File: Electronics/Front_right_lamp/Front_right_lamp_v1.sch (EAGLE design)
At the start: 9 parts

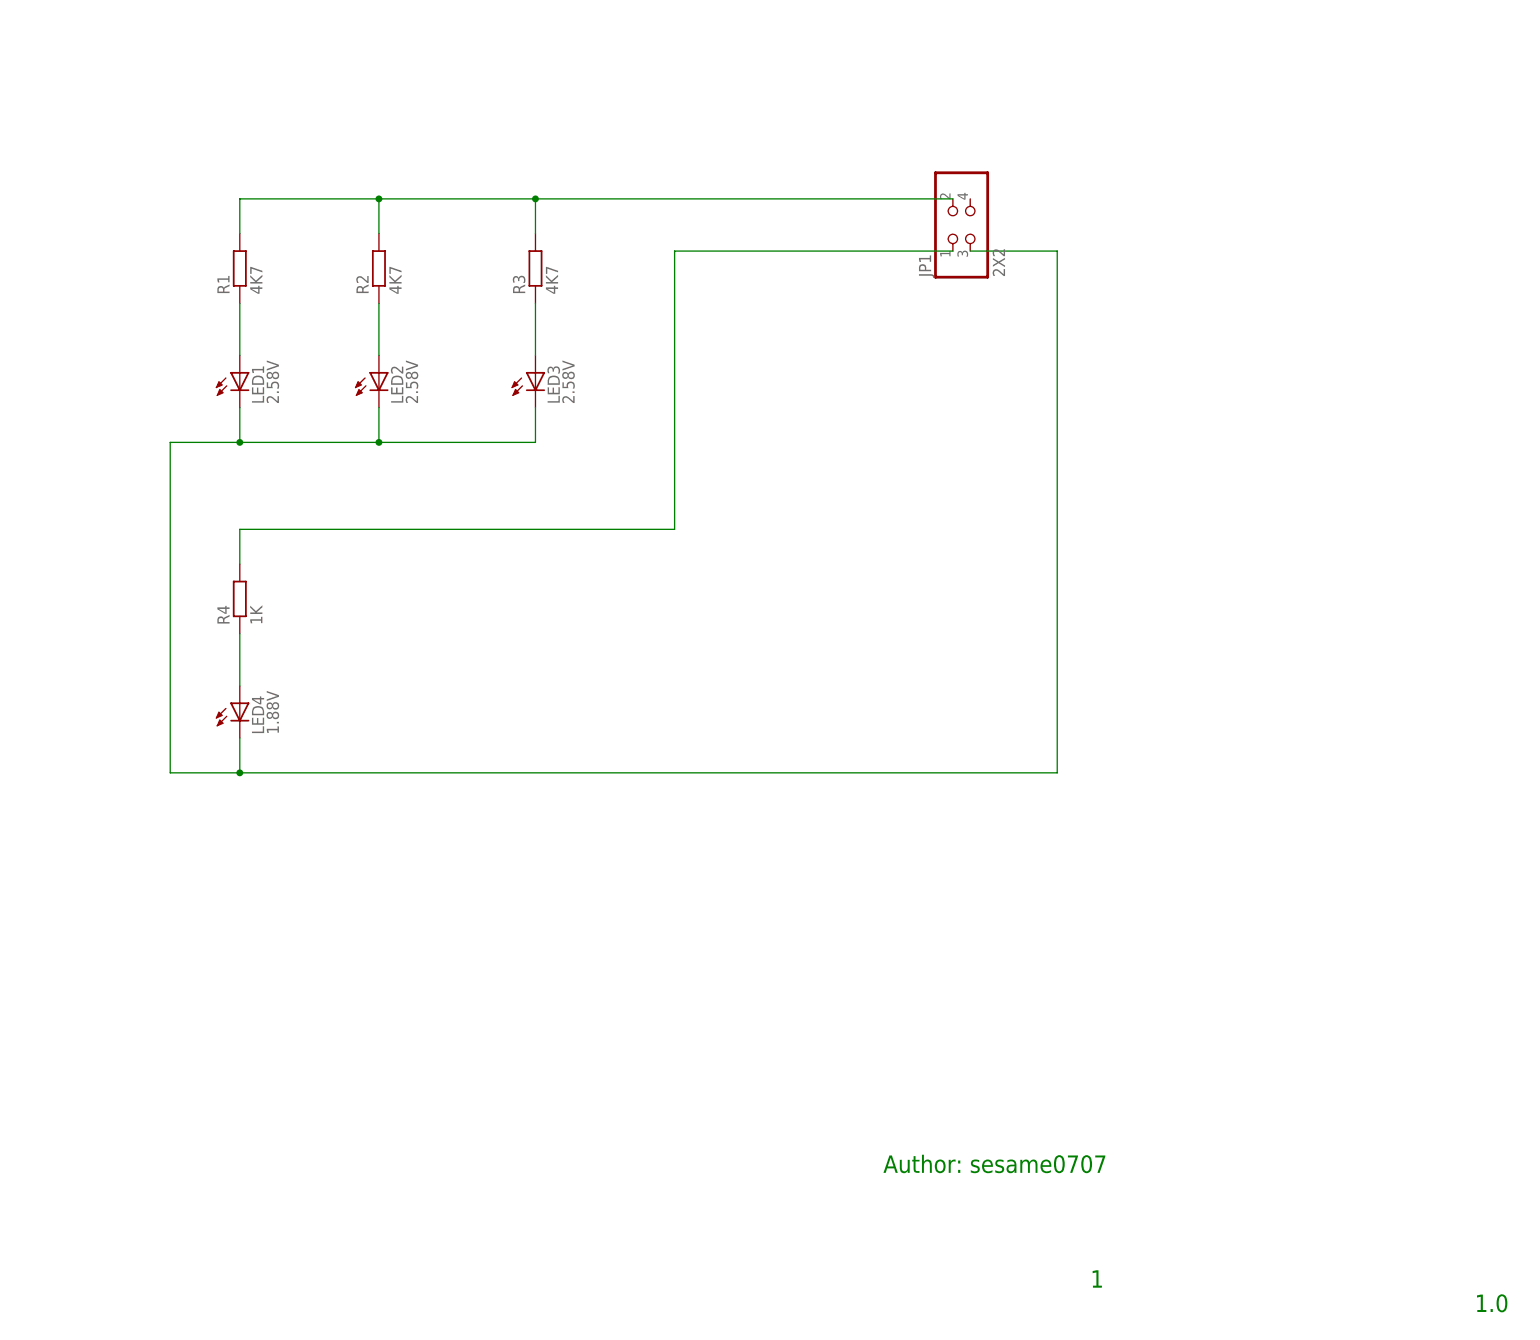
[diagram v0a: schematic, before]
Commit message: Front lamps done
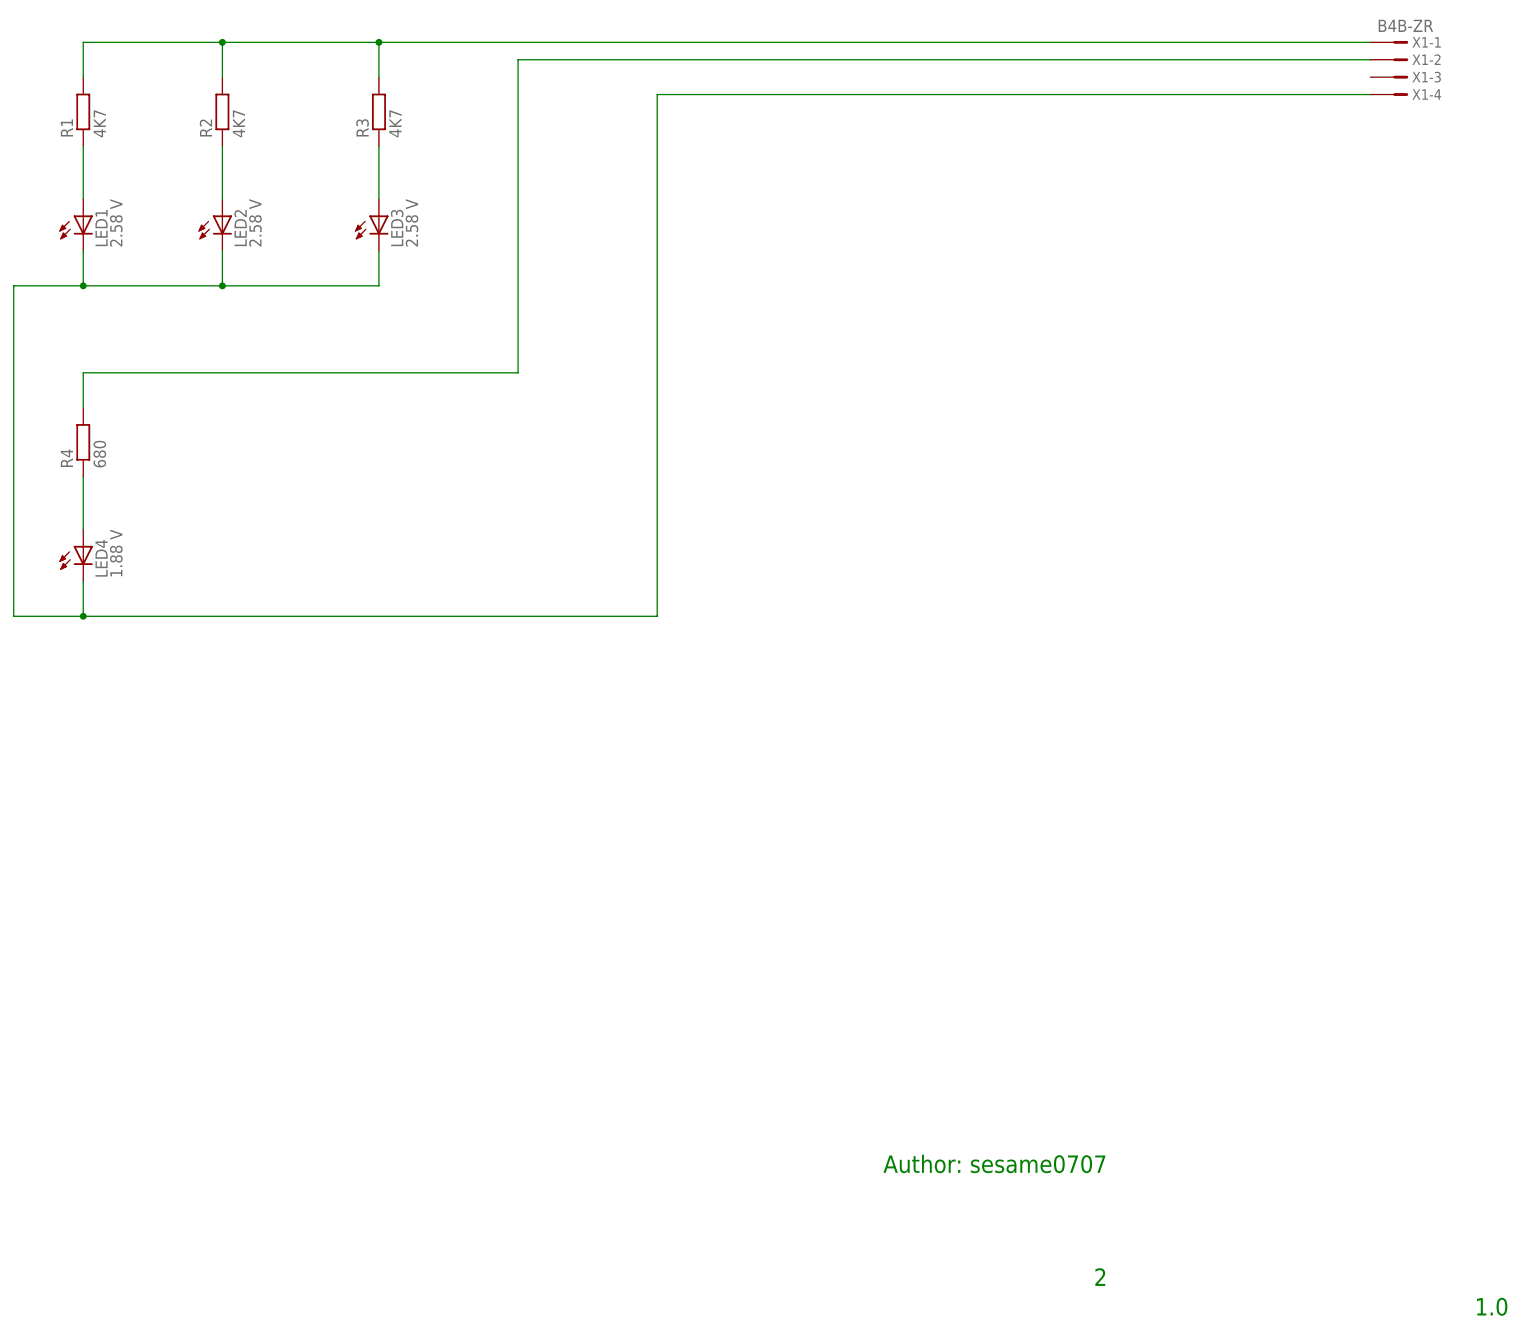
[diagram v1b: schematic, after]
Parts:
- removed JP1: 2X2, pinhead:PINHD-2X2
- added X1: B4B-ZR, con-jst:B4B-ZR
- LED1, LED2, LED3: value 2.58V -> 2.58 V; CURRENT (none) -> 0.14 mA
- LED4: value 1.88V -> 1.88 V; CURRENT (none) -> 1.42 mA
- R4: value 1K -> 680
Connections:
- net N$5: now also X1-1.1; no longer JP1.2
- net N$6: now also X1-2.1; no longer JP1.1
- net N$7: now also X1-4.1; no longer JP1.3
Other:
- note added: "2"
- note removed: "1"
- moved on the sheet: LED1, LED2, LED3, LED4, R1, R2, R3, R4
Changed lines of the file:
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@@
 <classes>
 <class number="0" name="default" width="0" drill="0">
+<clearance class="0" value="0.205"/>
 </class>
 </classes>
 <parts>
-<part name="FRAME1" library="frames" deviceset="FRAME_A_L" device="" value="Main"/>
-<part name="LED1" library="led" deviceset="LED" device="5MM" value="2.58V"/>
-<part name="LED2" library="led" deviceset="LED" device="5MM" value="2.58V"/>
-<part name="LED3" library="led" deviceset="LED" device="5MM" value="2.58V"/>
-<part name="LED4" library="led" deviceset="LED" device="5MM" value="1.88V"/>
+<part name="FRAME1" library="frames" deviceset="FRAME_A_L" device=""/>
+<part name="LED1" library="led" deviceset="LED" device="5MM" value="2.58 V">
+<attribute name="CURRENT" value="0.14 mA"/>
+</part>
+<part name="LED2" library="led" deviceset="LED" device="5MM" value="2.58 V">
+<attribute name="CURRENT" value="0.14 mA"/>
+</part>
+<part name="LED3" library="led" deviceset="LED" device="5MM" value="2.58 V">
+<attribute name="CURRENT" value="0.14 mA"/>
+</part>
+<part name="LED4" library="led" deviceset="LED" device="5MM" value="1.88 V">
+<attribute name="CURRENT" value="1.42 mA"/>
+</part>
 <part name="R1" library="resistor" deviceset="R-EU_" device="0204/2V" value="4K7"/>
 <part name="R2" library="resistor" deviceset="R-EU_" device="0204/2V" value="4K7"/>
 <part name="R3" library="resistor" deviceset="R-EU_" device="0204/2V" value="4K7"/>
-<part name="R4" library="resistor" deviceset="R-EU_" device="0204/2V" value="1K"/>
-<part name="JP1" library="pinhead" deviceset="PINHD-2X2" device="" value="2X2"/>
+<part name="R4" library="resistor" deviceset="R-EU_" device="0204/2V" value="680"/>
+<part name="X1" library="con-jst" deviceset="?4B-ZR" device="B"/>
 </parts>
 <sheets>
 <sheet>
 <plain>
-<text x="261.62" y="7.62" size="2.54" layer="91">1.0</text>
-<text x="205.486" y="11.176" size="2.54" layer="91">1</text>
 <text x="175.26" y="27.94" size="2.54" layer="91">Author: sesame0707</text>
+<text x="205.994" y="11.43" size="2.54" layer="91">2</text>
+<text x="261.62" y="7.112" size="2.54" layer="91">1.0</text>
 </plain>
 <instances>
 <instance part="FRAME1" gate="G$1" x="0" y="0"/>
 <instance part="FRAME1" gate="G$2" x="172.72" y="0"/>
-<instance part="LED1" gate="G$1" x="81.28" y="144.78"/>
-<instance part="LED2" gate="G$1" x="101.6" y="144.78"/>
-<instance part="LED3" gate="G$1" x="124.46" y="144.78"/>
-<instance part="LED4" gate="G$1" x="81.28" y="96.52"/>
-<instance part="R1" gate="G$1" x="81.28" y="160.02" rot="R90"/>
-<instance part="R2" gate="G$1" x="101.6" y="160.02" rot="R90"/>
-<instance part="R3" gate="G$1" x="124.46" y="160.02" rot="R90"/>
-<instance part="R4" gate="G$1" x="81.28" y="111.76" rot="R90"/>
-<instance part="JP1" gate="A" x="187.96" y="167.64" rot="R90"/>
+<instance part="LED1" gate="G$1" x="58.42" y="167.64">
+<attribute name="CURRENT" x="58.42" y="167.64" size="1.778" layer="96" display="off"/>
+</instance>
+<instance part="LED2" gate="G$1" x="78.74" y="167.64">
+<attribute name="CURRENT" x="78.74" y="167.64" size="1.778" layer="96" display="off"/>
+</instance>
+<instance part="LED3" gate="G$1" x="101.6" y="167.64">
+<attribute name="CURRENT" x="101.6" y="167.64" size="1.778" layer="96" display="off"/>
+</instance>
+<instance part="LED4" gate="G$1" x="58.42" y="119.38">
+<attribute name="CURRENT" x="58.42" y="119.38" size="1.778" layer="96" display="off"/>
+</instance>
+<instance part="R1" gate="G$1" x="58.42" y="182.88" rot="R90"/>
+<instance part="R2" gate="G$1" x="78.74" y="182.88" rot="R90"/>
+<instance part="R3" gate="G$1" x="101.6" y="182.88" rot="R90"/>
+<instance part="R4" gate="G$1" x="58.42" y="134.62" rot="R90"/>
+<instance part="X1" gate="-1" x="251.46" y="193.04"/>
+<instance part="X1" gate="-2" x="251.46" y="190.5"/>
+<instance part="X1" gate="-3" x="251.46" y="187.96"/>
+<instance part="X1" gate="-4" x="251.46" y="185.42"/>
 </instances>
 <busses>
@@
 <pinref part="R1" gate="G$1" pin="1"/>
 <pinref part="LED1" gate="G$1" pin="A"/>
-<wire x1="81.28" y1="154.94" x2="81.28" y2="147.32" width="0.1524" layer="91"/>
+<wire x1="58.42" y1="177.8" x2="58.42" y2="170.18" width="0.1524" layer="91"/>
 </segment>
 </net>
@@
 <pinref part="R2" gate="G$1" pin="1"/>
 <pinref part="LED2" gate="G$1" pin="A"/>
-<wire x1="101.6" y1="154.94" x2="101.6" y2="147.32" width="0.1524" layer="91"/>
+<wire x1="78.74" y1="177.8" x2="78.74" y2="170.18" width="0.1524" layer="91"/>
 </segment>
 </net>
@@
 <pinref part="R3" gate="G$1" pin="1"/>
 <pinref part="LED3" gate="G$1" pin="A"/>
-<wire x1="124.46" y1="154.94" x2="124.46" y2="147.32" width="0.1524" layer="91"/>
+<wire x1="101.6" y1="177.8" x2="101.6" y2="170.18" width="0.1524" layer="91"/>
 </segment>
 </net>
@@
 <pinref part="R4" gate="G$1" pin="1"/>
 <pinref part="LED4" gate="G$1" pin="A"/>
-<wire x1="81.28" y1="106.68" x2="81.28" y2="99.06" width="0.1524" layer="91"/>
+<wire x1="58.42" y1="129.54" x2="58.42" y2="121.92" width="0.1524" layer="91"/>
 </segment>
 </net>
@@
 <segment>
 <pinref part="R1" gate="G$1" pin="2"/>
-<wire x1="81.28" y1="165.1" x2="81.28" y2="170.18" width="0.1524" layer="91"/>
-<wire x1="81.28" y1="170.18" x2="101.6" y2="170.18" width="0.1524" layer="91"/>
+<wire x1="58.42" y1="187.96" x2="58.42" y2="193.04" width="0.1524" layer="91"/>
+<wire x1="58.42" y1="193.04" x2="78.74" y2="193.04" width="0.1524" layer="91"/>
 <pinref part="R2" gate="G$1" pin="2"/>
-<wire x1="101.6" y1="170.18" x2="124.46" y2="170.18" width="0.1524" layer="91"/>
-<wire x1="124.46" y1="170.18" x2="185.42" y2="170.18" width="0.1524" layer="91"/>
-<wire x1="101.6" y1="165.1" x2="101.6" y2="170.18" width="0.1524" layer="91"/>
-<junction x="101.6" y="170.18"/>
+<wire x1="78.74" y1="193.04" x2="101.6" y2="193.04" width="0.1524" layer="91"/>
+<wire x1="78.74" y1="187.96" x2="78.74" y2="193.04" width="0.1524" layer="91"/>
+<junction x="78.74" y="193.04"/>
 <pinref part="R3" gate="G$1" pin="2"/>
-<wire x1="124.46" y1="165.1" x2="124.46" y2="170.18" width="0.1524" layer="91"/>
-<junction x="124.46" y="170.18"/>
-<pinref part="JP1" gate="A" pin="2"/>
+<wire x1="101.6" y1="187.96" x2="101.6" y2="193.04" width="0.1524" layer="91"/>
+<junction x="101.6" y="193.04"/>
+<wire x1="101.6" y1="193.04" x2="246.38" y2="193.04" width="0.1524" layer="91"/>
+<pinref part="X1" gate="-1" pin="1"/>
 </segment>
 </net>
@@
 <segment>
 <pinref part="R4" gate="G$1" pin="2"/>
-<wire x1="81.28" y1="116.84" x2="81.28" y2="121.92" width="0.1524" layer="91"/>
-<wire x1="81.28" y1="121.92" x2="144.78" y2="121.92" width="0.1524" layer="91"/>
-<wire x1="144.78" y1="121.92" x2="144.78" y2="162.56" width="0.1524" layer="91"/>
-<pinref part="JP1" gate="A" pin="1"/>
-<wire x1="144.78" y1="162.56" x2="185.42" y2="162.56" width="0.1524" layer="91"/>
+<wire x1="58.42" y1="139.7" x2="58.42" y2="144.78" width="0.1524" layer="91"/>
+<wire x1="58.42" y1="144.78" x2="121.92" y2="144.78" width="0.1524" layer="91"/>
+<wire x1="121.92" y1="144.78" x2="121.92" y2="190.5" width="0.1524" layer="91"/>
+<wire x1="121.92" y1="190.5" x2="246.38" y2="190.5" width="0.1524" layer="91"/>
+<pinref part="X1" gate="-2" pin="1"/>
 </segment>
 </net>
@@
 <segment>
 <pinref part="LED1" gate="G$1" pin="C"/>
-<wire x1="81.28" y1="139.7" x2="81.28" y2="134.62" width="0.1524" layer="91"/>
-<wire x1="81.28" y1="134.62" x2="71.12" y2="134.62" width="0.1524" layer="91"/>
-<wire x1="71.12" y1="134.62" x2="71.12" y2="86.36" width="0.1524" layer="91"/>
-<wire x1="71.12" y1="86.36" x2="81.28" y2="86.36" width="0.1524" layer="91"/>
-<wire x1="81.28" y1="86.36" x2="200.66" y2="86.36" width="0.1524" layer="91"/>
-<wire x1="200.66" y1="86.36" x2="200.66" y2="162.56" width="0.1524" layer="91"/>
-<pinref part="JP1" gate="A" pin="3"/>
-<wire x1="200.66" y1="162.56" x2="187.96" y2="162.56" width="0.1524" layer="91"/>
-<wire x1="81.28" y1="134.62" x2="101.6" y2="134.62" width="0.1524" layer="91"/>
-<junction x="81.28" y="134.62"/>
+<wire x1="58.42" y1="162.56" x2="58.42" y2="157.48" width="0.1524" layer="91"/>
+<wire x1="58.42" y1="157.48" x2="48.26" y2="157.48" width="0.1524" layer="91"/>
+<wire x1="48.26" y1="157.48" x2="48.26" y2="109.22" width="0.1524" layer="91"/>
+<wire x1="48.26" y1="109.22" x2="58.42" y2="109.22" width="0.1524" layer="91"/>
+<wire x1="58.42" y1="157.48" x2="78.74" y2="157.48" width="0.1524" layer="91"/>
+<junction x="58.42" y="157.48"/>
 <pinref part="LED3" gate="G$1" pin="C"/>
-<wire x1="101.6" y1="134.62" x2="124.46" y2="134.62" width="0.1524" layer="91"/>
-<wire x1="124.46" y1="134.62" x2="124.46" y2="139.7" width="0.1524" layer="91"/>
+<wire x1="78.74" y1="157.48" x2="101.6" y2="157.48" width="0.1524" layer="91"/>
+<wire x1="101.6" y1="157.48" x2="101.6" y2="162.56" width="0.1524" layer="91"/>
 <pinref part="LED2" gate="G$1" pin="C"/>
-<wire x1="101.6" y1="139.7" x2="101.6" y2="134.62" width="0.1524" layer="91"/>
-<junction x="101.6" y="134.62"/>
+<wire x1="78.74" y1="162.56" x2="78.74" y2="157.48" width="0.1524" layer="91"/>
+<junction x="78.74" y="157.48"/>
 <pinref part="LED4" gate="G$1" pin="C"/>
-<wire x1="81.28" y1="91.44" x2="81.28" y2="86.36" width="0.1524" layer="91"/>
-<junction x="81.28" y="86.36"/>
+<wire x1="58.42" y1="114.3" x2="58.42" y2="109.22" width="0.1524" layer="91"/>
+<wire x1="58.42" y1="109.22" x2="142.24" y2="109.22" width="0.1524" layer="91"/>
+<wire x1="142.24" y1="109.22" x2="142.24" y2="185.42" width="0.1524" layer="91"/>
+<junction x="58.42" y="109.22"/>
+<wire x1="142.24" y1="185.42" x2="246.38" y2="185.42" width="0.1524" layer="91"/>
+<pinref part="X1" gate="-4" pin="1"/>
 </segment>
 </net>
